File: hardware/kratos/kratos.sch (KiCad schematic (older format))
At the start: 0 parts

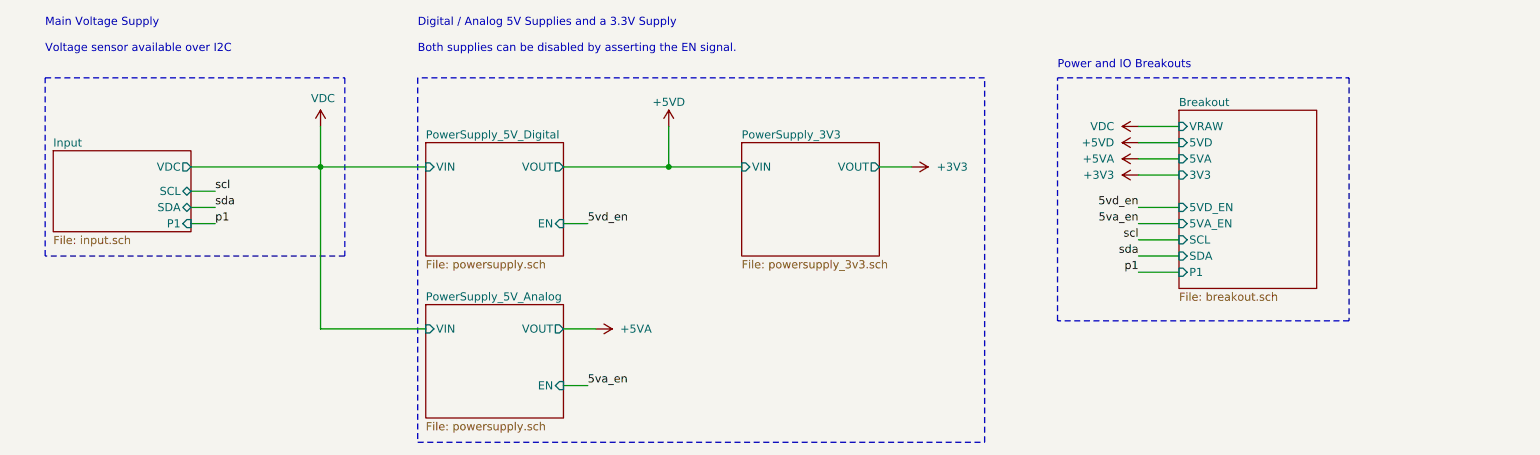
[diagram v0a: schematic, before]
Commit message: Update to linear regulators. Added PCB layout
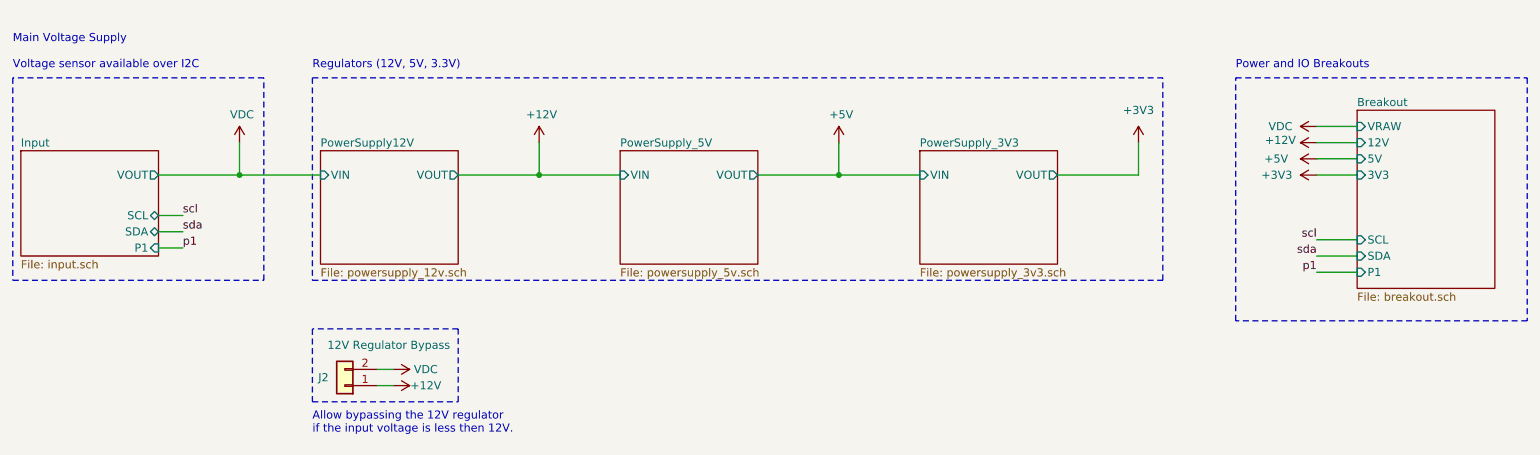
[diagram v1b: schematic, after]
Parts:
- added J2: 12V Regulator Bypass, Connector_PinHeader_2.54mm:PinHeader_1x02_P2.54mm_Vertical, symbol Connector_Generic:Conn_01x02
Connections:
- net VDC: now also J2.2 (Pin_2)
- new net +12V: J2.1 (Pin_1)
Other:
- note added: "Allow bypassing the 12V regulator\nif the input voltage is less then 12V."
- note added: "Regulators (12V, 5V, 3.3V)"
- note removed: "Digital / Analog 5V Supplies and a 3.3V Supply\n\nBoth supplies can be disabled by asserting the EN signal."

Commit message: Rev B
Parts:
- removed J2: 12V Regulator Bypass, Connector_PinHeader_2.54mm:PinHeader_1x02_P2.54mm_Vertical, symbol Connector_Generic:Conn_01x02
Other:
- note removed: "Allow bypassing the 12V regulator\nif the input voltage is less then 12V."

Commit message: REV C
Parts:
- added C1: 10uF, Capacitor_SMD:C_0805_2012Metric, symbol Device:C
- added C2: 10nF, Capacitor_SMD:C_0805_2012Metric, symbol Device:C
- added C3: 220uF, Capacitor_SMD:CP_Elec_6.3x5.4, symbol Device:CP
- added C4: 22uF, Capacitor_SMD:C_0805_2012Metric, symbol Device:C
- added D1: B340A, Diode_SMD:D_SMA, symbol Device:D_Schottky
- added D2: 5V, LED_SMD:LED_0805_2012Metric, symbol Device:LED
- added D3: 3V3, LED_SMD:LED_0805_2012Metric, symbol Device:LED
- added J1: BATT, drone:XT60, symbol Connector_Generic:Conn_01x02
- added J10: PWM4, Connector_PinSocket_2.54mm:PinSocket_1x03_P2.54mm_Vertical, symbol Connector_Generic:Conn_01x03
- added J11: PWM5, Connector_PinSocket_2.54mm:PinSocket_1x03_P2.54mm_Vertical, symbol Connector_Generic:Conn_01x03
- added J12: PWM6, Connector_PinSocket_2.54mm:PinSocket_1x03_P2.54mm_Vertical, symbol Connector_Generic:Conn_01x03
- added J13: 5V, Connector_PinSocket_2.54mm:PinSocket_1x05_P2.54mm_Vertical, symbol Connector_Generic:Conn_01x05
- added J14: 3V3, Connector_PinSocket_2.54mm:PinSocket_1x05_P2.54mm_Vertical, symbol Connector_Generic:Conn_01x05
- added J15: GND, Connector_PinSocket_2.54mm:PinSocket_1x05_P2.54mm_Vertical, symbol Connector_Generic:Conn_01x05
- added J2: RTR1, drone:XT60, symbol Connector_Generic:Conn_01x02
- added J3: RTR2, drone:XT60, symbol Connector_Generic:Conn_01x02
- added J4: RTR3, drone:XT60, symbol Connector_Generic:Conn_01x02
- added J5: RTR4, drone:XT60, symbol Connector_Generic:Conn_01x02
- added J6: VCC_SEL, Connector_PinSocket_2.54mm:PinSocket_2x02_P2.54mm_Vertical, symbol Connector_Generic:Conn_02x02_Top_Bottom
- added J7: PWM1, Connector_PinSocket_2.54mm:PinSocket_1x03_P2.54mm_Vertical, symbol Connector_Generic:Conn_01x03
- added J8: PWM2, Connector_PinSocket_2.54mm:PinSocket_1x03_P2.54mm_Vertical, symbol Connector_Generic:Conn_01x03
- added J9: PWM3, Connector_PinSocket_2.54mm:PinSocket_1x03_P2.54mm_Vertical, symbol Connector_Generic:Conn_01x03
- added L1: 15uH, inductors:MWSA0603S-150MT, symbol Device:L
- added R1, R2: 10k, Resistor_SMD:R_0805_2012Metric, symbol Device:R
- added R3: 3.24k, Resistor_SMD:R_0805_2012Metric, symbol Device:R
- added R4: 330, Resistor_SMD:R_0805_2012Metric, symbol Device:R
- added R5: 200, Resistor_SMD:R_0805_2012Metric, symbol Device:R
- added TP1: BATT, TestPoint:TestPoint_Pad_2.0x2.0mm, symbol Connector:TestPoint
- added TP2: 5V, TestPoint:TestPoint_Pad_2.0x2.0mm, symbol Connector:TestPoint
- added TP3: 3V3, TestPoint:TestPoint_Pad_2.0x2.0mm, symbol Connector:TestPoint
- added U1: TPS5430DDA, Package_SO:TI_SO-PowerPAD-8_ThermalVias, symbol Regulator_Switching:TPS5430DDA
- added U2: AMS1117-3.3, Package_TO_SOT_SMD:SOT-223-3_TabPin2, symbol Regulator_Linear:AMS1117-3.3
- added U3: ICARUS SHIELD, icarus:icarus-shield, symbol icarus:ICARUS
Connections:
- net +3V3: now also C4.1, J14.1 (Pin_1), J14.2 (Pin_2), J14.3 (Pin_3), J14.4 (Pin_4), J14.5 (Pin_5), J6.2 (Pin_2), R5.1, TP3.1, U2.2 (VO), U3.7 (3V3)
- net +5V: now also C3.1, J13.1 (Pin_1), J13.2 (Pin_2), J13.3 (Pin_3), J13.4 (Pin_4), J13.5 (Pin_5), J6.1 (Pin_1), L1.2, R2.1, R4.1, TP2.1, U2.3 (VI), U3.5 (5V)
- new net: C2.1, U1.1 (BOOT)
- new net: C2.2, D1.1 (K), L1.1, U1.8 (PH)
- new net: R2.2, R3.2, U1.4 (VSENSE)
- new net: R1.2, U1.5 (EN)
- new net: D2.2 (A), R4.2
- new net: D3.2 (A), R5.2
- new net +BATT: C1.1, J1.1 (Pin_1), J2.1 (Pin_1), J3.1 (Pin_1), J4.1 (Pin_1), J5.1 (Pin_1), R1.1, TP1.1, U1.7 (VIN), U3.1 (VDC), U3.3 (VDC)
- new net GND: C1.2, C3.2, C4.2, D1.2 (A), D2.1 (K), D3.1 (K), J1.2 (Pin_2), J10.3 (Pin_3), J11.3 (Pin_3), J12.3 (Pin_3), J15.1 (Pin_1), J15.2 (Pin_2), J15.3 (Pin_3), J15.4 (Pin_4), J15.5 (Pin_5), J2.2 (Pin_2), J3.2 (Pin_2), J4.2 (Pin_2), J5.2 (Pin_2), J7.3 (Pin_3), J8.3 (Pin_3), J9.3 (Pin_3), R3.1, U1.6 (GND), U1.9 (GNDPAD), U2.1 (GND), U3.2 (GND), U3.4 (GND), U3.6 (GND), U3.8 (GND)
- new net VCC: J10.2 (Pin_2), J11.2 (Pin_2), J12.2 (Pin_2), J6.3 (Pin_3), J6.4 (Pin_4), J7.2 (Pin_2), J8.2 (Pin_2), J9.2 (Pin_2)
- new net pwm1: J7.1 (Pin_1), U3.9 (PWM1)
- new net pwm2: J8.1 (Pin_1), U3.10 (PWM2)
- new net pwm3: J9.1 (Pin_1), U3.11 (PWM3)
- new net pwm4: J10.1 (Pin_1), U3.12 (PWM4)
- new net pwm5: J11.1 (Pin_1), U3.13 (PWM5)
- new net pwm6: J12.1 (Pin_1), U3.14 (PWM6)
- no-connect marks 0 -> 14
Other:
- note added: "2S - 6S Battery Input\n\n7.4V - 25.2V\n"
- note added: "3.3V Power Supply"
- note added: "5V Power Supply"
- note added: "A jumper for selecting which\nPWR rail the servos use"
- note added: "BATT Pads"
- note added: "Ceramic X5R/X7R"
- note added: "Input"
- note added: "PWM Servo Connectors"
- note added: "Power Breakout"
- note added: "Shield"
- note removed: "Main Voltage Supply\n\nVoltage sensor available over I2C\n"
- note removed: "Power and IO Breakouts"
- note removed: "Regulators (12V, 5V, 3.3V)"
